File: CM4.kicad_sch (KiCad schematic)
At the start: 11 parts, among them J11 Conn_02x05_Odd_Even, J6 HDMI_D_2.0, U1 RaspberryPi-CM4Lite, U2 DF40C-100DS-0.4V(51), U3 DF40C-100DS-0.4V(51)

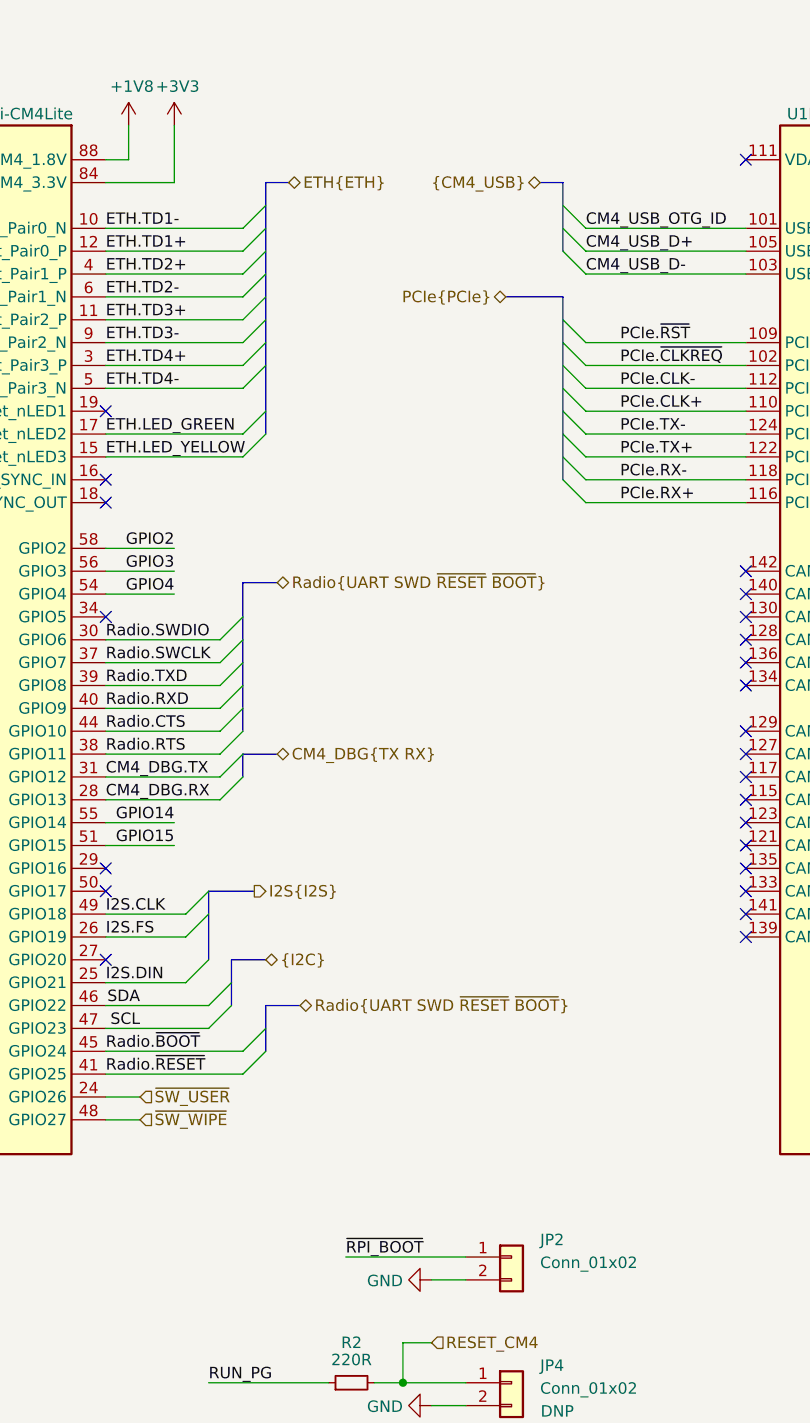
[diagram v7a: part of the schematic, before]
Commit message: initial rev 0.3:
updates
schematic:
-change usb current protection IC to 1.5A
-Added low-pass filter to the audio output
-PoE fixed primary windings polarity
-added option to select poe class with a jumper (between 3 and 4)
-fixes in poe design
-added testpoints
-added virtual hirose df40c connectors for pick and place use

lightblue.pretty:
-added fake DF40C footprint for pick and place and 3d model purposes

Signed-off-by: Dominik Sliwa <dominik@sliwa.io>
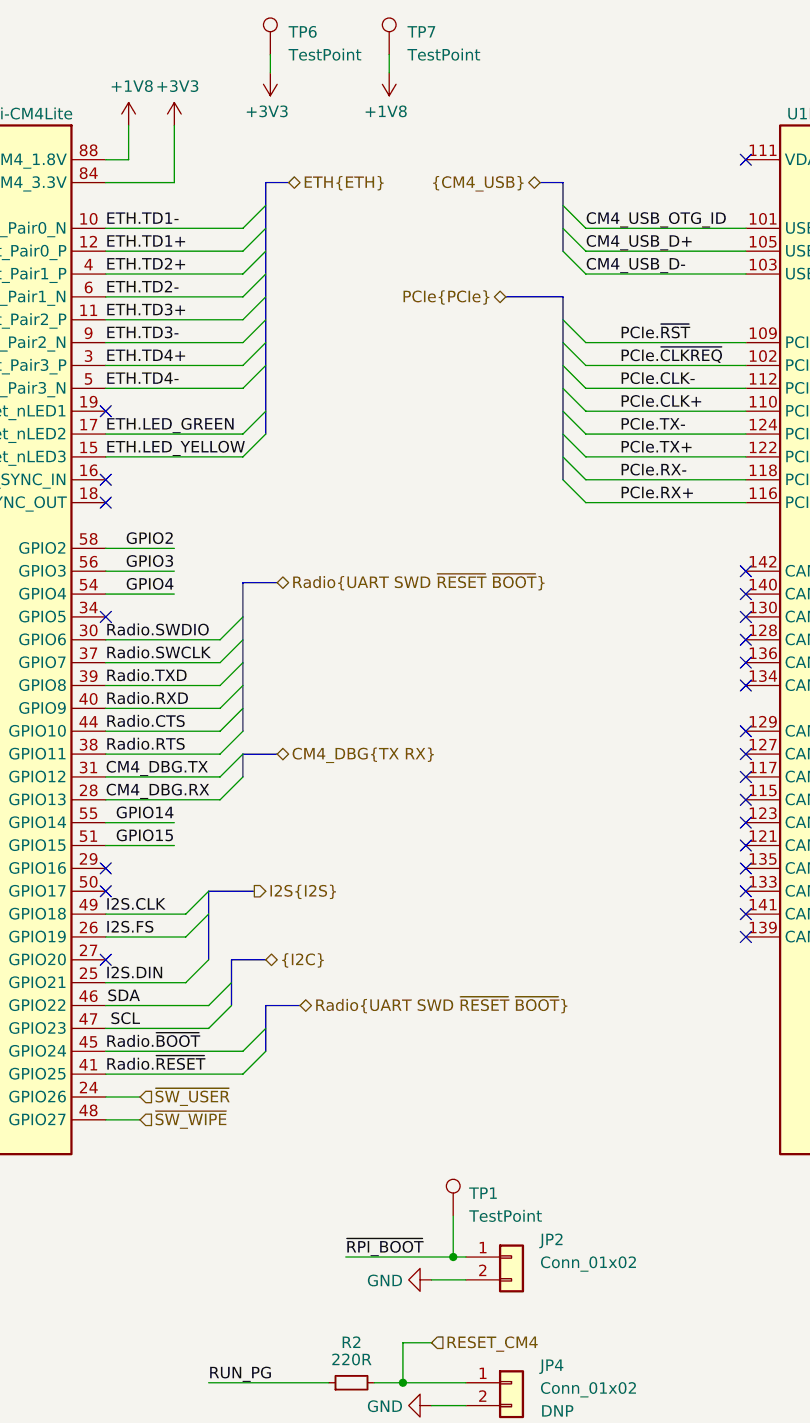
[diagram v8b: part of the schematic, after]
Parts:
- added TP1, TP6, TP7: TestPoint, TestPoint:TestPoint_Pad_D1.0mm, symbol Connector:TestPoint
- U2, U3: footprint (none) -> LightBlue:DF40C-100DS-0.4V51_virtual
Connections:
- net +1V8: now also TP7.1
- net +3V3: now also TP6.1
- net ~RPI_BOOT: now also TP1.1
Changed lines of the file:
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@@
   )
   (bus_alias "PCIe" (members "~RST" "~CLKREQ" "CLK+" "CLK-" "TX+" "TX-" "RX+" "RX-"))
-  (bus_alias "SD" (members "D[0..3]" "CMD" "CLK" "PWR" "DET"))
   (bus_alias "UART" (members "TXD" "RXD" "CTS" "RTS"))
   (bus_alias "HDMI" (members "D0+" "D0-" "D1+" "D1-" "D2+" "D2-" "CLK+" "CLK-" "CEC" "HPD" "SDA" "SCL"))
+  (bus_alias "SD" (members "D[0..3]" "CMD" "CLK" "PWR" "DET"))
   (junction (at 59.055 173.99) (diameter 0.9144) (color 0 0 0 0))
   (junction (at 121.92 171.45) (diameter 0.9144) (color 0 0 0 0))
+  (junction (at 127.508 157.48) (diameter 0.9144) (color 0 0 0 0))
   (junction (at 260.35 90.17) (diameter 1.016) (color 0 0 0 0))
   (junction (at 262.89 90.17) (diameter 1.016) (color 0 0 0 0))
@@
     (stroke (width 0) (type solid) (color 0 0 0 0))
   )
-  (wire (pts (xy 115.57 157.48) (xy 128.905 157.48))
+  (wire (pts (xy 107.188 23.876) (xy 107.188 25.908))
+    (stroke (width 0) (type solid) (color 0 0 0 0))
+  )
+  (wire (pts (xy 115.57 157.48) (xy 127.508 157.48))
     (stroke (width 0) (type solid) (color 0 0 0 0))
   )
@@
     (stroke (width 0) (type solid) (color 0 0 0 0))
   )
+  (wire (pts (xy 120.396 23.876) (xy 120.396 25.908))
+    (stroke (width 0) (type solid) (color 0 0 0 0))
+  )
   (wire (pts (xy 121.92 167.005) (xy 121.92 171.45))
     (stroke (width 0) (type solid) (color 0 0 0 0))
@@
   )
   (wire (pts (xy 125.095 185.42) (xy 128.905 185.42))
+    (stroke (width 0) (type solid) (color 0 0 0 0))
+  )
+  (wire (pts (xy 127.508 152.908) (xy 127.508 157.48))
+    (stroke (width 0) (type solid) (color 0 0 0 0))
+  )
+  (wire (pts (xy 127.508 157.48) (xy 128.905 157.48))
     (stroke (width 0) (type solid) (color 0 0 0 0))
   )
@@
     (pin "1")
   )
+  (symbol (lib_id "power:+3V3") (at 107.188 25.908 180) (unit 1)
+    (in_bom yes) (on_board yes)
+    (property "Reference" "#PWR0201" (id 0) (at 107.188 22.098 0)
+      (effects (font (size 1.27 1.27)) hide)
+    )
+    (property "Value" "+3V3" (id 1) (at 106.8197 30.2324 0))
+    (property "Footprint" "" (id 2) (at 107.188 25.908 0)
+      (effects (font (size 1.27 1.27)) hide)
+    )
+    (property "Datasheet" "" (id 3) (at 107.188 25.908 0)
+      (effects (font (size 1.27 1.27)) hide)
+    )
+    (pin "1")
+  )
+  (symbol (lib_id "power:+1V8") (at 120.396 25.908 180) (unit 1)
+    (in_bom yes) (on_board yes)
+    (property "Reference" "#PWR0202" (id 0) (at 120.396 22.098 0)
+      (effects (font (size 1.27 1.27)) hide)
+    )
+    (property "Value" "+1V8" (id 1) (at 120.0277 30.2324 0))
+    (property "Footprint" "" (id 2) (at 120.396 25.908 0)
+      (effects (font (size 1.27 1.27)) hide)
+    )
+    (property "Datasheet" "" (id 3) (at 120.396 25.908 0)
+      (effects (font (size 1.27 1.27)) hide)
+    )
+    (pin "1")
+  )
   (symbol (lib_id "power:+5V") (at 248.92 26.67 0) (unit 1)
     (in_bom yes) (on_board yes)
@@
     )
     (property "Datasheet" "" (id 3) (at 248.92 26.67 0)
+      (effects (font (size 1.27 1.27)) hide)
+    )
+    (pin "1")
+  )
+  (symbol (lib_id "Connector:TestPoint") (at 107.188 23.876 0) (unit 1)
+    (in_bom yes) (on_board yes) (fields_autoplaced)
+    (property "Reference" "TP6" (id 0) (at 109.22 21.3994 0)
+      (effects (font (size 1.27 1.27)) (justify left))
+    )
+    (property "Value" "TestPoint" (id 1) (at 109.22 23.9394 0)
+      (effects (font (size 1.27 1.27)) (justify left))
+    )
+    (property "Footprint" "TestPoint:TestPoint_Pad_D1.0mm" (id 2) (at 112.268 23.876 0)
+      (effects (font (size 1.27 1.27)) hide)
+    )
+    (property "Datasheet" "~" (id 3) (at 112.268 23.876 0)
+      (effects (font (size 1.27 1.27)) hide)
+    )
+    (pin "1")
+  )
+  (symbol (lib_id "Connector:TestPoint") (at 120.396 23.876 0) (unit 1)
+    (in_bom yes) (on_board yes) (fields_autoplaced)
+    (property "Reference" "TP7" (id 0) (at 122.428 21.3994 0)
+      (effects (font (size 1.27 1.27)) (justify left))
+    )
+    (property "Value" "TestPoint" (id 1) (at 122.428 23.9394 0)
+      (effects (font (size 1.27 1.27)) (justify left))
+    )
+    (property "Footprint" "TestPoint:TestPoint_Pad_D1.0mm" (id 2) (at 125.476 23.876 0)
+      (effects (font (size 1.27 1.27)) hide)
+    )
+    (property "Datasheet" "~" (id 3) (at 125.476 23.876 0)
+      (effects (font (size 1.27 1.27)) hide)
+    )
+    (pin "1")
+  )
+  (symbol (lib_id "Connector:TestPoint") (at 127.508 152.908 0) (unit 1)
+    (in_bom yes) (on_board yes) (fields_autoplaced)
+    (property "Reference" "TP1" (id 0) (at 129.286 150.4314 0)
+      (effects (font (size 1.27 1.27)) (justify left))
+    )
+    (property "Value" "TestPoint" (id 1) (at 129.286 152.9714 0)
+      (effects (font (size 1.27 1.27)) (justify left))
+    )
+    (property "Footprint" "TestPoint:TestPoint_Pad_D1.0mm" (id 2) (at 132.588 152.908 0)
+      (effects (font (size 1.27 1.27)) hide)
+    )
+    (property "Datasheet" "~" (id 3) (at 132.588 152.908 0)
       (effects (font (size 1.27 1.27)) hide)
     )
@@
   )
   (symbol (lib_id "LightBlue:DF40C-100DS-0.4V(51)") (at 254 128.27 0) (unit 1)
-    (in_bom yes) (on_board no)
+    (in_bom yes) (on_board yes)
     (property "Reference" "U2" (id 0) (at 254.635 121.285 0))
     (property "Value" "DF40C-100DS-0.4V(51)" (id 1) (at 254.635 123.825 0))
-    (property "Footprint" "" (id 2) (at 254 128.27 0)
+    (property "Footprint" "LightBlue:DF40C-100DS-0.4V51_virtual" (id 2) (at 254 128.27 0)
       (effects (font (size 1.27 1.27)) hide)
     )
@@
   )
   (symbol (lib_id "LightBlue:DF40C-100DS-0.4V(51)") (at 254 139.065 0) (unit 1)
-    (in_bom yes) (on_board no)
+    (in_bom yes) (on_board yes)
     (property "Reference" "U3" (id 0) (at 254.635 132.715 0))
     (property "Value" "DF40C-100DS-0.4V(51)" (id 1) (at 254.635 135.255 0))
-    (property "Footprint" "" (id 2) (at 254 139.065 0)
+    (property "Footprint" "LightBlue:DF40C-100DS-0.4V51_virtual" (id 2) (at 254 139.065 0)
       (effects (font (size 1.27 1.27)) hide)
     )
@@
       (effects (font (size 1.27 1.27)) hide)
     )
-    (property "Datasheet" "https://datasheets.raspberrypi.org/cm4/cm4-datasheet.pdf" (id 3) (at 63.5 88.9 0)
-      (effects (font (size 1.27 1.27)) hide)
-    )
+    (property "Datasheet" "" (id 3) (at 63.5 88.9 0)
+      (effects (font (size 1.27 1.27)) hide)
+    )
